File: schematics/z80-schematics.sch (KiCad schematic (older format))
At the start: 32 parts

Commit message: Added serial I/O
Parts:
- added JP?: USB POWER, symbol JUMPER
- added P?: FTDI SERIAL, symbol CONN_6
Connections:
- net labels added: /cts, /rts, /siosel, rxd, txd
- wire segments 263 -> 267
- no-connect marks 7 -> 19
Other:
- moved on the sheet: U?

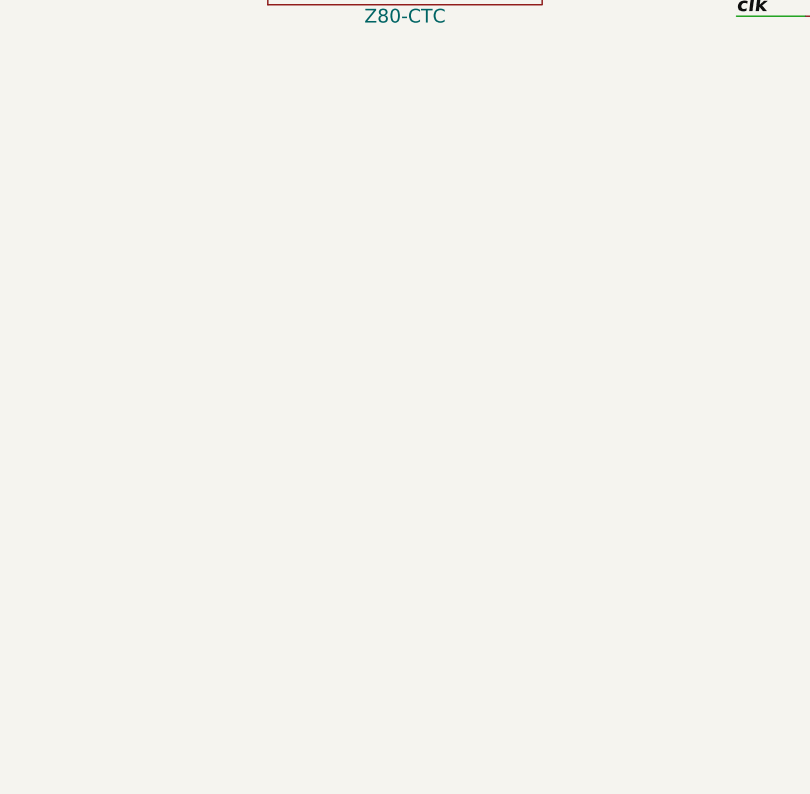
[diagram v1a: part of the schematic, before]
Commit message: Added (incomplete) general I/O buffers.
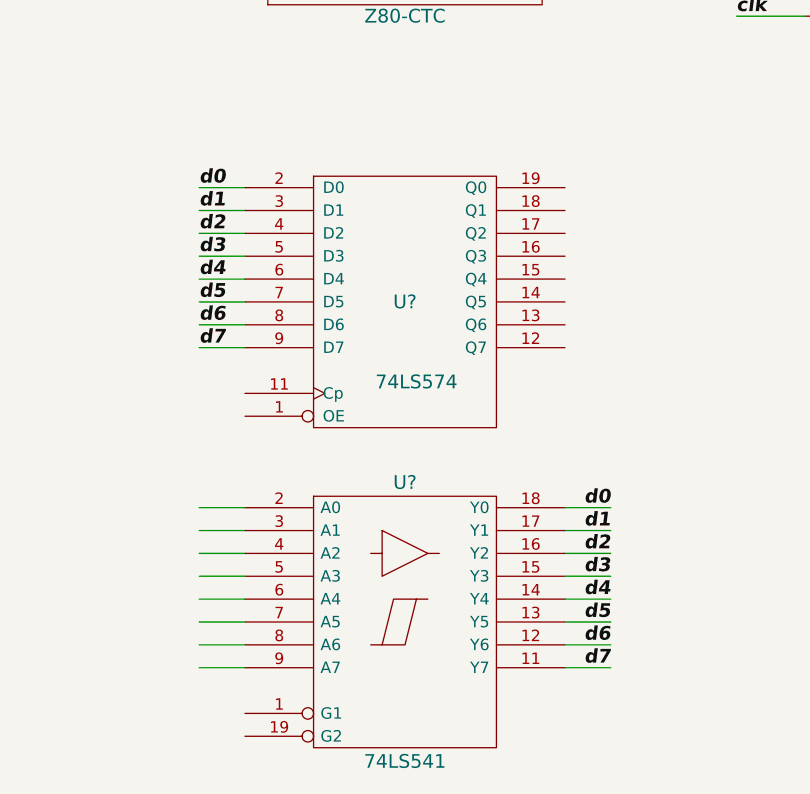
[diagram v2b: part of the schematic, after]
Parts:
- added U?: 74LS574, symbol 74LS574
- added U?: 74LS541, symbol 74LS541
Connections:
- wire segments 267 -> 291

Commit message: Added decoupling caps.
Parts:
- removed C?: C, symbol C
- added C? (x14): C, symbol C
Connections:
- wire segments 291 -> 360

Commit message: Added component identifiers to the schematic
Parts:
- gave numbers to parts that had none: 46

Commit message: Update schematics to newer version of kicad
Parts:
- C1, C10, C11, C12, C13, C14, C15, C2, C3, C4, C5, C6, C7, C8, C9: symbol C -> C-RESCUE-z80-schematics
- D1: symbol LED -> LED-RESCUE-z80-schematics
- R1, R10, R11, R12, R2, R3, R4, R5, R6, R7, R8, R9: symbol R -> R-RESCUE-z80-schematics
- U3: symbol 28C256 -> 28C256-RESCUE-z80-schematics
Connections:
- wire segments 360 -> 323
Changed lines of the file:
@@
 EESchema Schematic File Version 2
+LIBS:z80-schematics-rescue
 LIBS:power
 LIBS:device
@@
 LIBS:memory
 LIBS:xilinx
-LIBS:special
 LIBS:microcontrollers
 LIBS:dsp
@@
 LIBS:simon
 LIBS:xo-14s
-EELAYER 27 0
+LIBS:z80-schematics-cache
+EELAYER 25 0
 EELAYER END
 $Descr A3 16535 11693
@@
 $EndDescr
 $Comp
-L 28C256 U3
+L 28C256-RESCUE-z80-schematics U3
 U 1 1 54359578
 P 1700 1750
@@
 d7
 $Comp
-L R R1
+L R-RESCUE-z80-schematics R1
 U 1 1 5436F625
 P 14850 2450
@@
 $EndComp
 $Comp
-L R R2
+L R-RESCUE-z80-schematics R2
 U 1 1 5436F632
 P 14850 2600
@@
 $EndComp
 $Comp
-L R R3
+L R-RESCUE-z80-schematics R3
 U 1 1 5436F638
 P 14850 2750
@@
 $EndComp
 $Comp
-L R R4
+L R-RESCUE-z80-schematics R4
 U 1 1 5436F63E
 P 14850 2900
@@
 $EndComp
 $Comp
-L R R5
+L R-RESCUE-z80-schematics R5
 U 1 1 5436F644
 P 14850 3050
@@
 $EndComp
 $Comp
-L R R6
+L R-RESCUE-z80-schematics R6
 U 1 1 5436F64A
 P 14850 3200
@@
 $EndComp
 $Comp
-L R R7
+L R-RESCUE-z80-schematics R7
 U 1 1 5436F650
 P 14850 3350
@@
 $EndComp
 $Comp
-L R R8
+L R-RESCUE-z80-schematics R8
 U 1 1 5436F656
 P 14850 3500
@@
 /b19
 $Comp
-L LED D1
+L LED-RESCUE-z80-schematics D1
 U 1 1 5439CDAB
 P 1000 4650
@@
 $EndComp
 $Comp
-L R R9
+L R-RESCUE-z80-schematics R9
 U 1 1 5439CDBF
 P 1000 5500
@@
 $EndComp
 $Comp
-L R R10
+L R-RESCUE-z80-schematics R10
 U 1 1 5439CDD1
 P 1550 4650
@@
 $EndComp
 $Comp
-L R R11
+L R-RESCUE-z80-schematics R11
 U 1 1 5439CDDC
 P 2250 4650
@@
 $EndComp
 $Comp
-L C C15
+L C-RESCUE-z80-schematics C15
 U 1 1 5439CE08
 P 2100 5500
@@
 $EndComp
 $Comp
-L GND #PWR?
+L GND-RESCUE-z80-schematics #PWR?
 U 1 1 5439D0D3
 P 2250 6050
@@
 $EndComp
 $Comp
-L GND #PWR?
+L GND-RESCUE-z80-schematics #PWR?
 U 1 1 5439D495
 P 1550 6050
@@
 $EndComp
 $Comp
-L GND #PWR?
+L GND-RESCUE-z80-schematics #PWR?
 U 1 1 5439D762
 P 1000 6050
@@
 $EndComp
 $Comp
-L GND #PWR?
+L GND-RESCUE-z80-schematics #PWR?
 U 1 1 5439DA28
 P 3500 6050
@@
 $EndComp
 $Comp
-L R R12
+L R-RESCUE-z80-schematics R12
 U 1 1 54443E36
 P 3000 4650
@@
 $EndComp
 $Comp
-L GND #PWR?
+L GND-RESCUE-z80-schematics #PWR?
 U 1 1 54444BB8
 P 10150 6500
@@
 /rts
 $Comp
-L GND #PWR?
+L GND-RESCUE-z80-schematics #PWR?
 U 1 1 54445AE6
 P 11350 5000
@@
 	12200 3350 11750 3350
 Wire Wire Line
-	14300 3950 14400 3950
-Wire Wire Line
-	14400 3950 14850 3950
+	14300 3950 14850 3950
 Wire Wire Line
 	14400 3950 14400 4350
@@
 	800  3550 1100 3550
 Wire Wire Line
-	3450 3350 3450 3450
-Wire Wire Line
-	3450 3450 3450 3550
+	3450 3350 3450 3550
 Wire Wire Line
 	3450 3450 3150 3450
@@
 	15300 3350 15100 3350
 Wire Wire Line
-	15300 2300 15300 2450
-Wire Wire Line
-	15300 2450 15300 2600
-Wire Wire Line
-	15300 2600 15300 2750
-Wire Wire Line
-	15300 2750 15300 2900
-Wire Wire Line
-	15300 2900 15300 3050
-Wire Wire Line
-	15300 3050 15300 3200
-Wire Wire Line
-	15300 3200 15300 3350
-Wire Wire Line
-	15300 3350 15300 3500
+	15300 2300 15300 3500
 Wire Wire Line
 	15100 3200 15300 3200
@@
 	2400 5900 2400 5800
 Wire Wire Line
-	2100 5900 2250 5900
-Wire Wire Line
-	2250 5900 2400 5900
+	2100 5900 2400 5900
 Wire Wire Line
 	2100 5900 2100 5700
@@
 	2400 5050 2400 5200
 Wire Wire Line
-	2100 5050 2250 5050
-Wire Wire Line
-	2250 5050 2400 5050
-Wire Wire Line
-	2400 5050 2800 5050
+	2100 5050 2800 5050
 Wire Wire Line
 	2100 5050 2100 5300
@@
 	2250 4400 2250 4250
 Wire Wire Line
-	1550 4900 1550 5050
-Wire Wire Line
-	1550 5050 1550 5200
+	1550 4900 1550 5200
 Wire Wire Line
 	1550 5800 1550 6050
@@
 d7
 $Comp
-L C C1
+L C-RESCUE-z80-schematics C1
 U 1 1 54448997
 P 1000 6800
@@
 $EndComp
 $Comp
-L C C2
+L C-RESCUE-z80-schematics C2
 U 1 1 544489AB
 P 1300 6800
@@
 $EndComp
 $Comp
-L C C3
+L C-RESCUE-z80-schematics C3
 U 1 1 544489BF
 P 1600 6800
@@
 $EndComp
 $Comp
-L C C4
+L C-RESCUE-z80-schematics C4
 U 1 1 544489D3
 P 1900 6800
@@
 $EndComp
 $Comp
-L C C5
+L C-RESCUE-z80-schematics C5
 U 1 1 544489E7
 P 2200 6800
@@
 $EndComp
 $Comp
-L C C6
+L C-RESCUE-z80-schematics C6
 U 1 1 544489FB
 P 2500 6800
@@
 $EndComp
 $Comp
-L C C7
+L C-RESCUE-z80-schematics C7
 U 1 1 54448A0F
 P 2800 6800
@@
 $EndComp
 $Comp
-L C C8
+L C-RESCUE-z80-schematics C8
 U 1 1 54448A23
 P 1000 7800
@@
 $EndComp
 $Comp
-L C C9
+L C-RESCUE-z80-schematics C9
 U 1 1 54448A37
 P 1300 7800
@@
 $EndComp
 $Comp
-L C C10
+L C-RESCUE-z80-schematics C10
 U 1 1 54448A4B
 P 1600 7800
@@
 $EndComp
 $Comp
-L C C11
+L C-RESCUE-z80-schematics C11
 U 1 1 54448A5F
 P 1900 7800
@@
 $EndComp
 $Comp
-L C C12
+L C-RESCUE-z80-schematics C12
 U 1 1 54448A73
 P 2200 7800
@@
 $EndComp
 $Comp
-L C C13
+L C-RESCUE-z80-schematics C13
 U 1 1 54448A87
 P 2500 7800
@@
 $EndComp
 $Comp
-L C C14
+L C-RESCUE-z80-schematics C14
 U 1 1 54448A9B
 P 2800 7800
@@
 	1000 6600 1000 6500
 Wire Wire Line
-	1000 6500 1300 6500
-Wire Wire Line
-	1300 6500 1600 6500
-Wire Wire Line
-	1600 6500 1900 6500
-Wire Wire Line
-	1900 6500 2200 6500
-Wire Wire Line
-	2200 6500 2500 6500
-Wire Wire Line
-	2500 6500 2800 6500
+	1000 6500 2800 6500
 Wire Wire Line
 	2800 6500 2800 6600
@@
 Connection ~ 1600 6500
 Wire Wire Line
-	1900 6400 1900 6500
-Wire Wire Line
-	1900 6500 1900 6600
+	1900 6400 1900 6600
 Connection ~ 1900 6500
 Wire Wire Line
@@
 	1000 7000 1000 7100
 Wire Wire Line
-	1000 7100 1300 7100
-Wire Wire Line
-	1300 7100 1600 7100
-Wire Wire Line
-	1600 7100 1900 7100
-Wire Wire Line
-	1900 7100 2200 7100
-Wire Wire Line
-	2200 7100 2500 7100
-Wire Wire Line
-	2500 7100 2800 7100
+	1000 7100 2800 7100
 Wire Wire Line
 	2800 7100 2800 7000
@@
 Connection ~ 1600 7100
 Wire Wire Line
-	1900 7000 1900 7100
-Wire Wire Line
-	1900 7100 1900 7200
+	1900 7000 1900 7200
 Connection ~ 1900 7100
 Wire Wire Line
@@
 $EndComp
 $Comp
-L GND #PWR?
+L GND-RESCUE-z80-schematics #PWR?
 U 1 1 54449B07
 P 1900 7200
@@
 	1000 7600 1000 7500
 Wire Wire Line
-	1000 7500 1300 7500
-Wire Wire Line
-	1300 7500 1600 7500
-Wire Wire Line
-	1600 7500 1900 7500
-Wire Wire Line
-	1900 7500 2200 7500
-Wire Wire Line
-	2200 7500 2500 7500
-Wire Wire Line
-	2500 7500 2800 7500
+	1000 7500 2800 7500
 Wire Wire Line
 	2800 7500 2800 7600
@@
 Connection ~ 1600 7500
 Wire Wire Line
-	1900 7400 1900 7500
-Wire Wire Line
-	1900 7500 1900 7600
+	1900 7400 1900 7600
 Connection ~ 1900 7500
 Wire Wire Line
@@
 	1000 8000 1000 8100
 Wire Wire Line
-	1000 8100 1300 8100
-Wire Wire Line
-	1300 8100 1600 8100
-Wire Wire Line
-	1600 8100 1900 8100
-Wire Wire Line
-	1900 8100 2200 8100
-Wire Wire Line
-	2200 8100 2500 8100
-Wire Wire Line
-	2500 8100 2800 8100
+	1000 8100 2800 8100
 Wire Wire Line
 	2800 8100 2800 8000
@@
 Connection ~ 2200 8100
 Wire Wire Line
-	1900 8000 1900 8100
-Wire Wire Line
-	1900 8100 1900 8200
+	1900 8000 1900 8200
 Connection ~ 1900 8100
 Wire Wire Line
@@
 $EndComp
 $Comp
-L GND #PWR?
+L GND-RESCUE-z80-schematics #PWR?
 U 1 1 5444ACAB
 P 1900 8200

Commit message: Label schematics with values
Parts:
- C1: value C -> 10u
- C10, C11, C12, C13, C14, C2, C3, C4, C5, C6, C7, C8, C9: value C -> 0.1u
- R12: value R -> 10K
- U12: value 74LS574 -> 74HC574
- U13: value 74LS541 -> 74HC541
- U2: value 628128 -> AS6C1008
- U3: value 28C256 -> CAT28C256BL
- U6: value 74LS138 -> 74HC138
- U7: value 74LS540 -> 74HCT540
- U8: value 7400 -> 74HCT00
- U9: value 74LS32 -> 74HCT32
- X1: value XO-14S -> XO-14S 2MHz
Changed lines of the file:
@@
 P 1700 1750
 F 0 "U3" H 1900 2750 70  0000 C CNN
-F 1 "28C256" H 2000 750 70  0000 C CNN
+F 1 "CAT28C256BL" H 2000 750 70  0000 C CNN
 F 2 "" H 1700 1750 60  0000 C CNN
 F 3 "" H 1700 1750 60  0000 C CNN
@@
 P 4200 1850
 F 0 "U2" H 4250 1850 70  0000 C CNN
-F 1 "628128" H 4500 650 70  0000 C CNN
+F 1 "AS6C1008" H 4500 650 70  0000 C CNN
 F 2 "" H 4200 1850 60  0000 C CNN
 F 3 "" H 4200 1850 60  0000 C CNN
@@
 P 10150 2100
 F 0 "U6" H 10250 2600 60  0000 C CNN
-F 1 "74LS138" H 10300 1551 60  0000 C CNN
+F 1 "74HC138" H 10300 1551 60  0000 C CNN
 F 2 "~" H 10150 2100 60  0000 C CNN
 F 3 "~" H 10150 2100 60  0000 C CNN
@@
 P 12900 2950
 F 0 "U7" H 12900 2750 60  0000 C CNN
-F 1 "74LS540" H 12900 2650 60  0000 C CNN
+F 1 "74HCT540" H 12900 2650 60  0000 C CNN
 F 2 "~" H 12900 2950 60  0000 C CNN
 F 3 "~" H 12900 2950 60  0000 C CNN
@@
 P 13700 3950
 F 0 "U8" H 13700 4000 60  0000 C CNN
-F 1 "7400" H 13700 3850 60  0000 C CNN
+F 1 "74HCT00" H 13700 3850 60  0000 C CNN
 F 2 "~" H 13700 3950 60  0000 C CNN
 F 3 "~" H 13700 3950 60  0000 C CNN
@@
 P 13700 4650
 F 0 "U8" H 13700 4700 60  0000 C CNN
-F 1 "7400" H 13700 4550 60  0000 C CNN
+F 1 "74HCT00" H 13700 4550 60  0000 C CNN
 F 2 "~" H 13700 4650 60  0000 C CNN
 F 3 "~" H 13700 4650 60  0000 C CNN
@@
 P 13700 5150
 F 0 "U9" H 13700 5200 60  0000 C CNN
-F 1 "74LS32" H 13700 5100 60  0000 C CNN
+F 1 "74HCT32" H 13700 5100 60  0000 C CNN
 F 2 "~" H 13700 5150 60  0000 C CNN
 F 3 "~" H 13700 5150 60  0000 C CNN
@@
 P 1700 3450
 F 0 "U9" H 1700 3500 60  0000 C CNN
-F 1 "74LS32" H 1700 3400 60  0000 C CNN
+F 1 "74HCT32" H 1700 3400 60  0000 C CNN
 F 2 "~" H 1700 3450 60  0000 C CNN
 F 3 "~" H 1700 3450 60  0000 C CNN
@@
 P 4050 3450
 F 0 "U8" H 4050 3500 60  0000 C CNN
-F 1 "7400" H 4050 3350 60  0000 C CNN
+F 1 "74HCT00" H 4050 3350 60  0000 C CNN
 F 2 "~" H 4050 3450 60  0000 C CNN
 F 3 "~" H 4050 3450 60  0000 C CNN
@@
 P 4100 5050
 F 0 "X1" H 3860 5410 60  0000 C CNN
-F 1 "XO-14S" H 4100 4680 60  0000 C CNN
+F 1 "XO-14S 2MHz" H 4100 4680 60  0000 C CNN
 F 2 "" H 4100 5050 60  0000 C CNN
 F 3 "" H 4100 5050 60  0000 C CNN
@@
 P 3000 4650
 F 0 "R12" V 3080 4650 40  0000 C CNN
-F 1 "R" V 3007 4651 40  0000 C CNN
+F 1 "10K" V 3007 4651 40  0000 C CNN
 F 2 "" V 2930 4650 30  0000 C CNN
 F 3 "" H 3000 4650 30  0000 C CNN
@@
 P 7600 7300
 F 0 "U12" H 7600 7300 60  0000 C CNN
-F 1 "74LS574" H 7650 6950 60  0000 C CNN
+F 1 "74HC574" H 7650 6950 60  0000 C CNN
 F 2 "" H 7600 7300 60  0000 C CNN
 F 3 "" H 7600 7300 60  0000 C CNN
@@
 P 7600 8700
 F 0 "U13" H 7600 9275 60  0000 C BNN
-F 1 "74LS541" H 7600 8125 60  0000 C TNN
+F 1 "74HC541" H 7600 8125 60  0000 C TNN
 F 2 "" H 7600 8700 60  0000 C CNN
 F 3 "" H 7600 8700 60  0000 C CNN
@@
 P 1000 6800
 F 0 "C1" H 1000 6900 40  0000 L CNN
-F 1 "C" H 1006 6715 40  0000 L CNN
+F 1 "10u" H 1006 6715 40  0000 L CNN
 F 2 "" H 1038 6650 30  0000 C CNN
 F 3 "" H 1000 6800 60  0000 C CNN
@@
 P 1300 6800
 F 0 "C2" H 1300 6900 40  0000 L CNN
-F 1 "C" H 1306 6715 40  0000 L CNN
+F 1 "0.1u" H 1306 6715 40  0000 L CNN
 F 2 "" H 1338 6650 30  0000 C CNN
 F 3 "" H 1300 6800 60  0000 C CNN
@@
 P 1600 6800
 F 0 "C3" H 1600 6900 40  0000 L CNN
-F 1 "C" H 1606 6715 40  0000 L CNN
+F 1 "0.1u" H 1606 6715 40  0000 L CNN
 F 2 "" H 1638 6650 30  0000 C CNN
 F 3 "" H 1600 6800 60  0000 C CNN
@@
 P 1900 6800
 F 0 "C4" H 1900 6900 40  0000 L CNN
-F 1 "C" H 1906 6715 40  0000 L CNN
+F 1 "0.1u" H 1906 6715 40  0000 L CNN
 F 2 "" H 1938 6650 30  0000 C CNN
 F 3 "" H 1900 6800 60  0000 C CNN
@@
 P 2200 6800
 F 0 "C5" H 2200 6900 40  0000 L CNN
-F 1 "C" H 2206 6715 40  0000 L CNN
+F 1 "0.1u" H 2206 6715 40  0000 L CNN
 F 2 "" H 2238 6650 30  0000 C CNN
 F 3 "" H 2200 6800 60  0000 C CNN
@@
 P 2500 6800
 F 0 "C6" H 2500 6900 40  0000 L CNN
-F 1 "C" H 2506 6715 40  0000 L CNN
+F 1 "0.1u" H 2506 6715 40  0000 L CNN
 F 2 "" H 2538 6650 30  0000 C CNN
 F 3 "" H 2500 6800 60  0000 C CNN
@@
 P 2800 6800
 F 0 "C7" H 2800 6900 40  0000 L CNN
-F 1 "C" H 2806 6715 40  0000 L CNN
+F 1 "0.1u" H 2806 6715 40  0000 L CNN
 F 2 "" H 2838 6650 30  0000 C CNN
 F 3 "" H 2800 6800 60  0000 C CNN
@@
 P 1000 7800
 F 0 "C8" H 1000 7900 40  0000 L CNN
-F 1 "C" H 1006 7715 40  0000 L CNN
+F 1 "0.1u" H 1006 7715 40  0000 L CNN
 F 2 "" H 1038 7650 30  0000 C CNN
 F 3 "" H 1000 7800 60  0000 C CNN
@@
 P 1300 7800
 F 0 "C9" H 1300 7900 40  0000 L CNN
-F 1 "C" H 1306 7715 40  0000 L CNN
+F 1 "0.1u" H 1306 7715 40  0000 L CNN
 F 2 "" H 1338 7650 30  0000 C CNN
 F 3 "" H 1300 7800 60  0000 C CNN
@@
 P 1600 7800
 F 0 "C10" H 1600 7900 40  0000 L CNN
-F 1 "C" H 1606 7715 40  0000 L CNN
+F 1 "0.1u" H 1606 7715 40  0000 L CNN
 F 2 "" H 1638 7650 30  0000 C CNN
 F 3 "" H 1600 7800 60  0000 C CNN
@@
 P 1900 7800
 F 0 "C11" H 1900 7900 40  0000 L CNN
-F 1 "C" H 1906 7715 40  0000 L CNN
+F 1 "0.1u" H 1906 7715 40  0000 L CNN
 F 2 "" H 1938 7650 30  0000 C CNN
 F 3 "" H 1900 7800 60  0000 C CNN
@@
 P 2200 7800
 F 0 "C12" H 2200 7900 40  0000 L CNN
-F 1 "C" H 2206 7715 40  0000 L CNN
+F 1 "0.1u" H 2206 7715 40  0000 L CNN
 F 2 "" H 2238 7650 30  0000 C CNN
 F 3 "" H 2200 7800 60  0000 C CNN
@@
 P 2500 7800
 F 0 "C13" H 2500 7900 40  0000 L CNN
-F 1 "C" H 2506 7715 40  0000 L CNN
+F 1 "0.1u" H 2506 7715 40  0000 L CNN
 F 2 "" H 2538 7650 30  0000 C CNN
 F 3 "" H 2500 7800 60  0000 C CNN
@@
 P 2800 7800
 F 0 "C14" H 2800 7900 40  0000 L CNN
-F 1 "C" H 2806 7715 40  0000 L CNN
+F 1 "0.1u" H 2806 7715 40  0000 L CNN
 F 2 "" H 2838 7650 30  0000 C CNN
 F 3 "" H 2800 7800 60  0000 C CNN

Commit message: Fix accidental DRC failures
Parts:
- X1: symbol XO-14S -> XO-14S-RESCUE-z80-schematics
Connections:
- net labels added: +5V, VSS
- wire segments 323 -> 331
- no-connect marks 19 -> 40

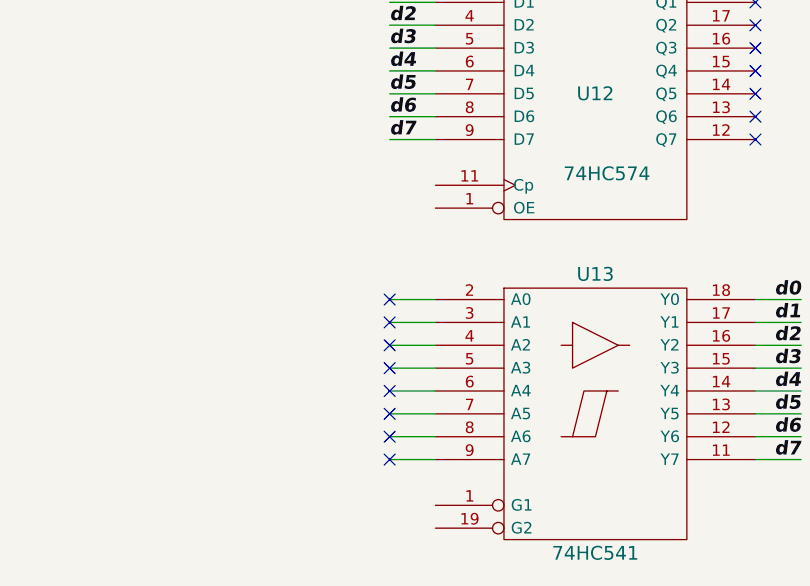
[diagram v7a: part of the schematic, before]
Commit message: Fix DRC and fill in pull-ups on incomplete I/O circuitry
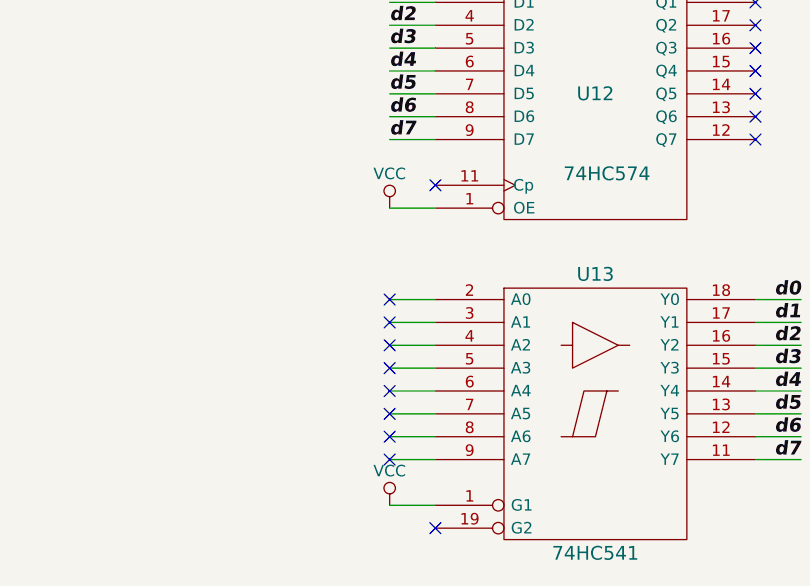
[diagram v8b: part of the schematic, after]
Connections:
- net +5V: now also U12.1 (OE), U13.1 (G1)
- no-connect marks 40 -> 42
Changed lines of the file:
@@
 LIBS:memory
 LIBS:xilinx
-LIBS:microcontrollers
-LIBS:dsp
-LIBS:microchip
-LIBS:analog_switches
-LIBS:motorola
-LIBS:texas
-LIBS:intel
-LIBS:audio
-LIBS:interface
-LIBS:digital-audio
-LIBS:philips
-LIBS:display
-LIBS:cypress
-LIBS:siliconi
-LIBS:opto
-LIBS:atmel
-LIBS:contrib
-LIBS:valves
-LIBS:o_zilog
-LIBS:simon
-LIBS:xo-14s
 LIBS:z80-schematics-cache
 EELAYER 25 0
@@
 	3750 7000 3750 7100
 Connection ~ 3500 7000
+$Comp
+L VCC #PWR?
+U 1 1 5725E77F
+P 6700 7800
+F 0 "#PWR?" H 6700 7650 50  0001 C CNN
+F 1 "VCC" H 6700 7950 50  0000 C CNN
+F 2 "" H 6700 7800 50  0000 C CNN
+F 3 "" H 6700 7800 50  0000 C CNN
+	1    6700 7800
+	1    0    0    -1
+$EndComp
+Wire Wire Line
+	6900 7800 6700 7800
+NoConn ~ 6900 7700
+$Comp
+L VCC #PWR?
+U 1 1 5725EC6B
+P 6700 9100
+F 0 "#PWR?" H 6700 8950 50  0001 C CNN
+F 1 "VCC" H 6700 9250 50  0000 C CNN
+F 2 "" H 6700 9100 50  0000 C CNN
+F 3 "" H 6700 9100 50  0000 C CNN
+	1    6700 9100
+	1    0    0    -1
+$EndComp
+Wire Wire Line
+	6700 9100 6900 9100
+NoConn ~ 6900 9200
 $EndSCHEMATC
